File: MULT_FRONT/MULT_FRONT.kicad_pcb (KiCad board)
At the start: 2 copper layers, 20.2 x 43.2 mm, 12 parts, among them J1 Screw_Terminal_01x01, J10 Screw_Terminal_01x01, J11 Screw_Terminal_01x01, J12 Screw_Terminal_01x01, J2 Screw_Terminal_01x01, J3 Screw_Terminal_01x01, J4 Screw_Terminal_01x01, J5 Screw_Terminal_01x01, J6 Screw_Terminal_01x01, J7 Screw_Terminal_01x01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

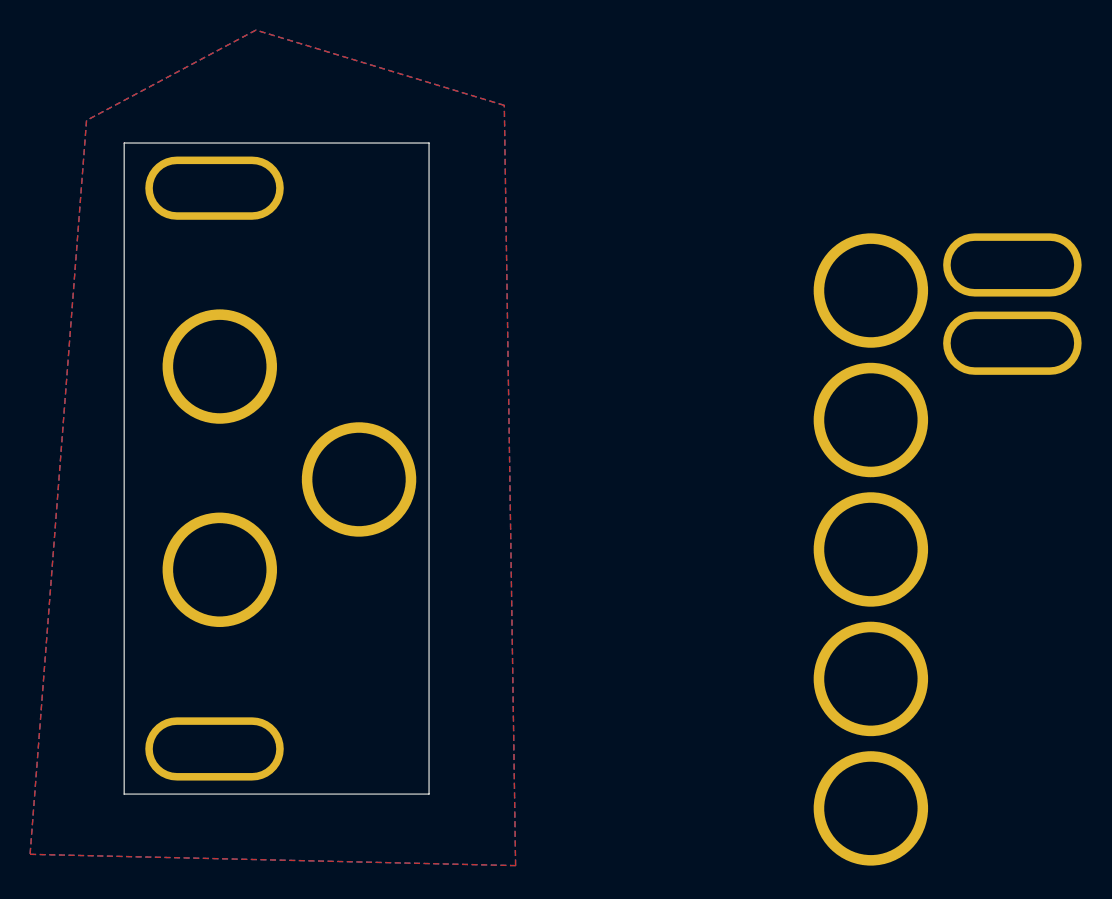
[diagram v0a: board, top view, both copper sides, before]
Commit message: Create MULT front panel
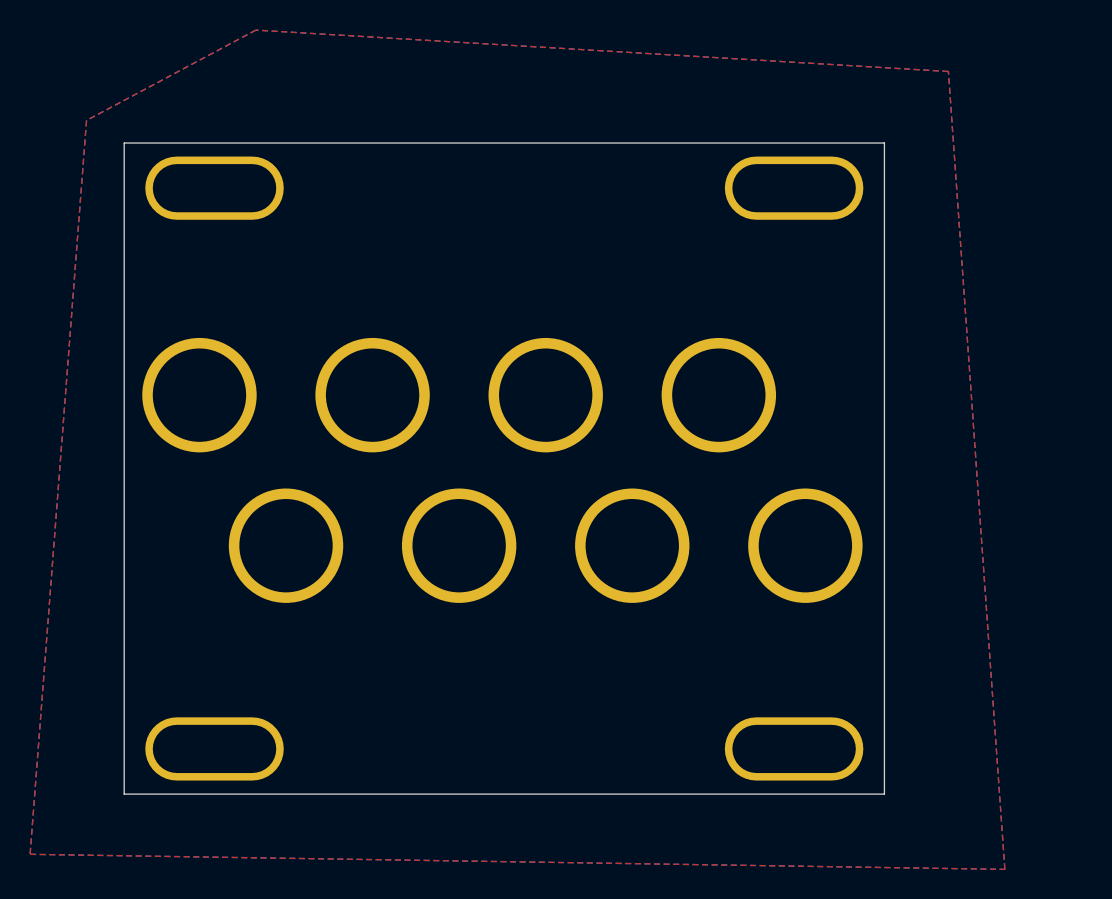
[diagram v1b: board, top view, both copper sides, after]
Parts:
- moved J7 30.6 mm to (144.5, 115.2)
- moved J11 28.7 mm to (128.0, 91.8)
- moved J10 27.4 mm to (122.2, 101.8)
- moved J12 18.0 mm to (145.2, 101.8)
- moved J9 17.9 mm to (133.8, 101.8)
- moved J6 15.4 mm to (144.5, 78.0)
- moved J8 12.3 mm to (139.5, 91.8)
- moved J3 5.67 mm to (116.5, 91.8)
- moved J2 4.68 mm to (110.8, 101.8)
- moved J1 2.33 mm to (105.0, 91.8)
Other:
- board size 20.2 x 43.2 mm -> 50.5 x 43.2 mm
- board text added: "MULT"
